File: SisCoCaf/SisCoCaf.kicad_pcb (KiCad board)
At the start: 2 copper layers, 20 parts, among them IC1 LPC111X_102, J1 Conn_01x02_Female, J2 Conn_01x02_Female, J3 Conn_01x03_Male, J4 Conn_01x03_Male, J5 Conn_01x01_Male, Q1 BC547, Q2 BC547, U1 LM317_TO39, U2 NRF24L01_Breakout

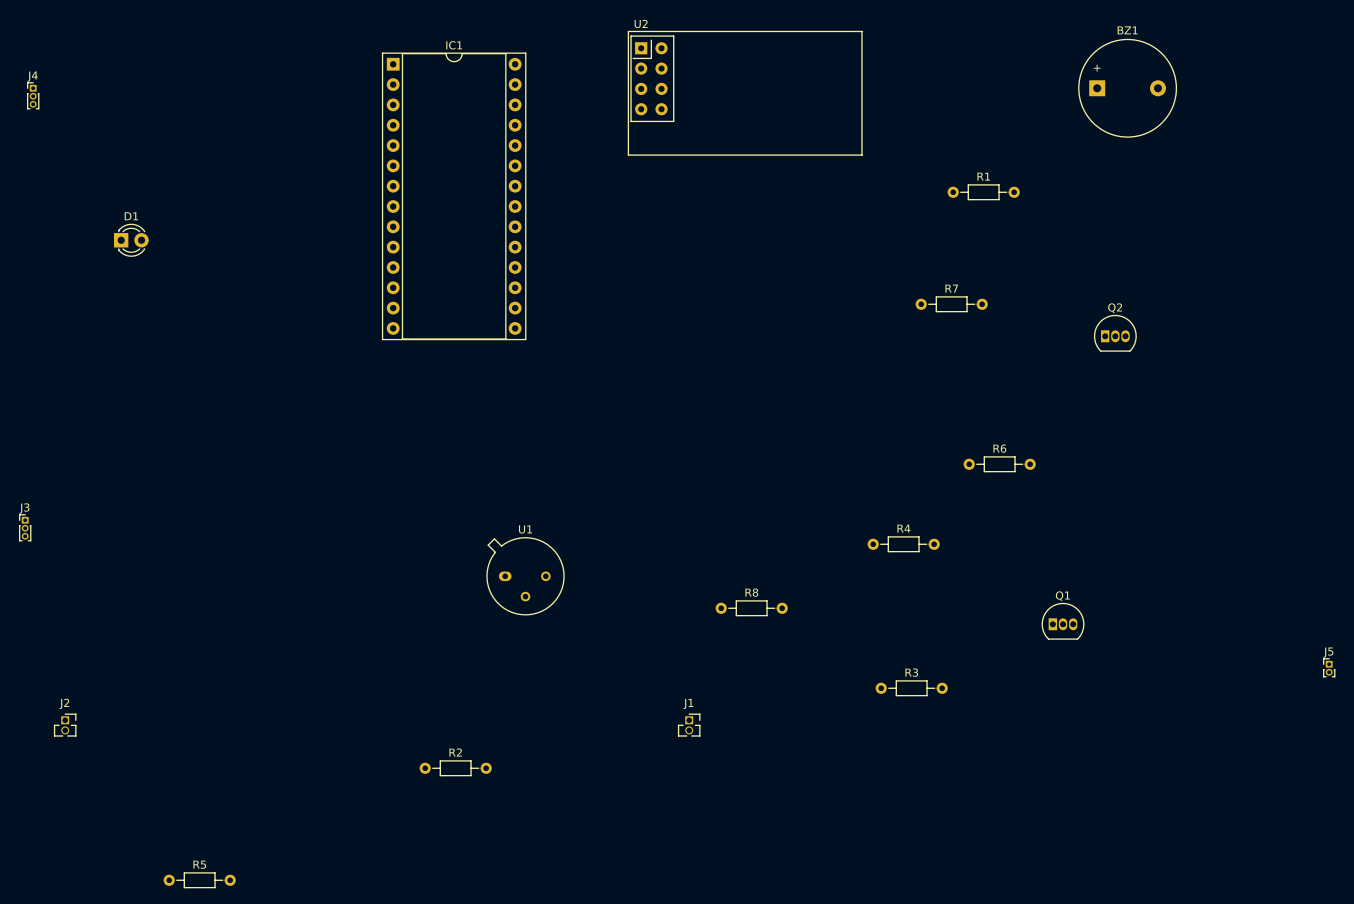
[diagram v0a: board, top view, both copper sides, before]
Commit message: Esquemático corregido. PCB v1.0
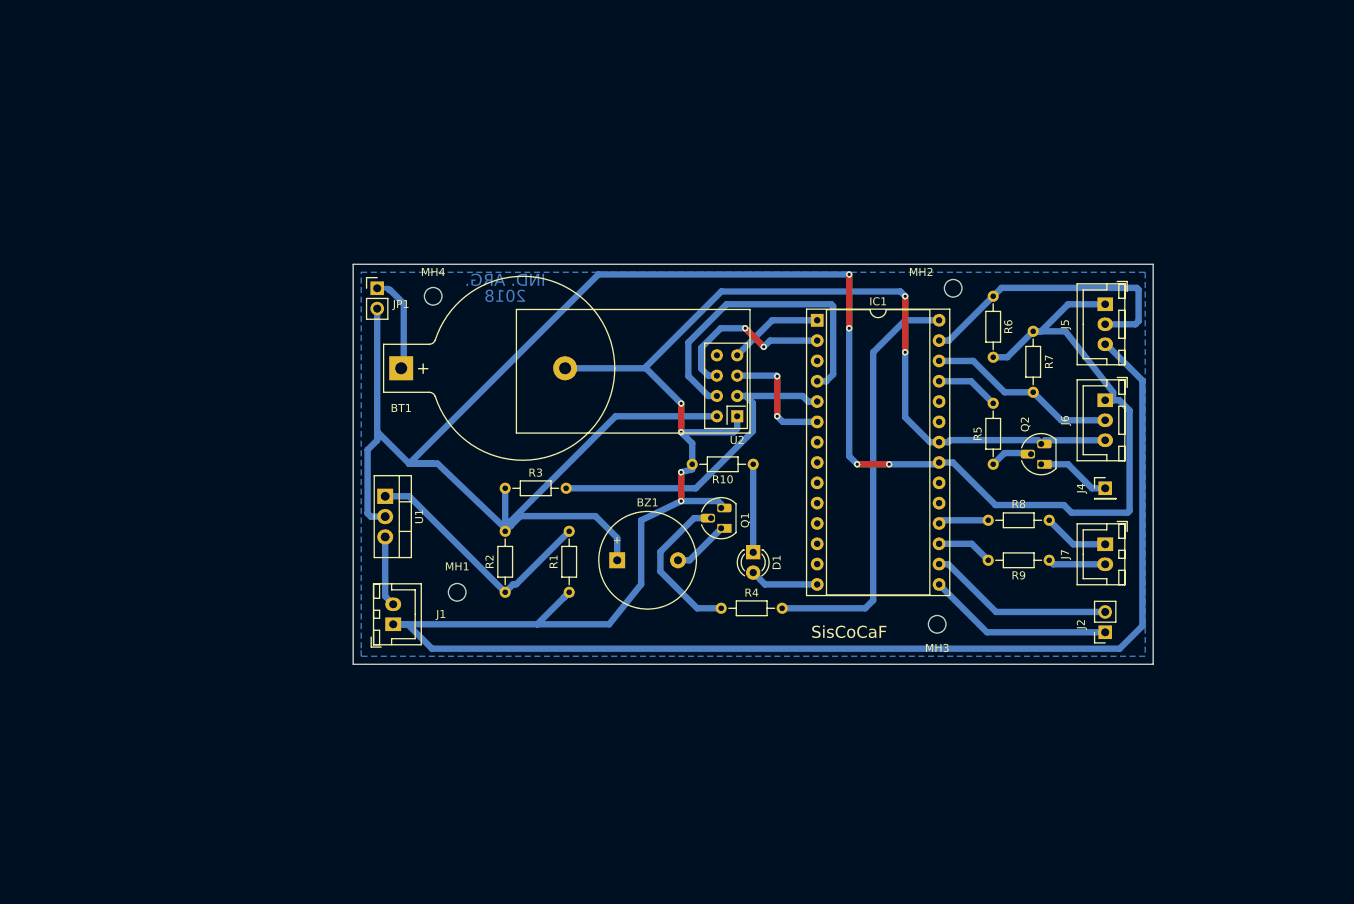
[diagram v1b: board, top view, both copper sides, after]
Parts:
- removed J3: Conn_01x03_Male, Connector_PinHeader_1.00mm:PinHeader_1x03_P1.00mm_Vertical
- added BT1: Battery_Cell, Battery:BatteryHolder_Keystone_103_1x20mm, F.Cu at (99.0, 90.0)
- added J6: Conn_01x03_Male, Connector_JST:JST_XH_B03B-XH-A_1x03_P2.50mm_Vertical, F.Cu at (187.0, 94.0)
- added J7: Conn_01x02_Male, Connector_JST:JST_XH_B02B-XH-A_1x02_P2.50mm_Vertical, F.Cu at (187.0, 112.0)
- added JP1: Jumper, Connector_PinHeader_2.54mm:PinHeader_1x02_P2.54mm_Vertical, F.Cu at (96.0, 80.0)
- added MH1: MountingHole, MountingHole:MountingHole_2.2mm_M2, F.Cu at (106.0, 118.0)
- added MH2: MountingHole, MountingHole:MountingHole_2.2mm_M2, F.Cu at (168.0, 80.0)
- added MH3: MountingHole, MountingHole:MountingHole_2.2mm_M2, F.Cu at (166.0, 122.0)
- added MH4: MountingHole, MountingHole:MountingHole_2.2mm_M2, F.Cu at (103.0, 81.0)
- added R10: 220, Resistor_THT:R_Axial_DIN0204_L3.6mm_D1.6mm_P7.62mm_Horizontal, F.Cu at (143.0, 102.0)
- added R9: 220, Resistor_THT:R_Axial_DIN0204_L3.6mm_D1.6mm_P7.62mm_Horizontal, F.Cu at (180.0, 114.0)
- J1: value Conn_01x02_Female -> Entrada; footprint Connector_PinSocket_1.27mm:PinSocket_1x02_P1.27mm_Vertical -> Connector_JST:JST_XH_B02B-XH-A_1x02_P2.50mm_Vertical
- J2: footprint Connector_PinSocket_1.27mm:PinSocket_1x02_P1.27mm_Vertical -> Connector_PinSocket_2.54mm:PinSocket_1x02_P2.54mm_Vertical
- J4: value Conn_01x03_Male -> Conn_01x01_Male; footprint Connector_PinHeader_1.00mm:PinHeader_1x03_P1.00mm_Vertical -> Connector_PinHeader_2.54mm:PinHeader_1x01_P2.54mm_Vertical
- J5: value Conn_01x01_Male -> Conn_01x03_Male; footprint Connector_PinHeader_1.00mm:PinHeader_1x02_P1.00mm_Vertical -> Connector_JST:JST_XH_B03B-XH-A_1x03_P2.50mm_Vertical
- Q1, Q2: footprint Package_TO_SOT_THT:TO-92_Inline -> Package_TO_SOT_THT:TO-92_HandSolder
- R6, R7: value 220 -> 4k7
- U1: footprint Package_TO_SOT_THT:TO-39-3 -> Package_TO_SOT_THT:TO-220-3_Vertical
- moved J4 143.0 mm to (187.0, 105.0)
- moved J2 130.5 mm to (187.0, 123.0), turned to 180 degrees
- moved R5 115.4 mm to (173.0, 102.0), turned to 90 degrees
- moved D1 88.1 mm to (143.0, 113.0), turned to 270 degrees
- moved BZ1 84.1 mm to (126.0, 114.0)
- moved R1 69.3 mm to (120.0, 118.0), turned to 90 degrees
- moved IC1 61.9 mm to (151.0, 84.0)
- moved R3 53.2 mm to (112.0, 105.0)
- moved J5 53.0 mm to (187.0, 82.0), turned to 270 degrees
- moved U2 47.5 mm to (141.0, 96.0), turned to 180 degrees
- moved Q1 43.2 mm to (139.0, 110.0), turned to 90 degrees
- moved R8 42.4 mm to (180.0, 109.0), turned to 180 degrees
- moved J1 38.9 mm to (98.0, 122.0), turned to 90 degrees
- moved R2 24.2 mm to (112.0, 118.0), turned to 90 degrees
- moved R6 21.2 mm to (173.0, 81.0), turned to 270 degrees
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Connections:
- net Net-(D1-Pad2) renamed /LED
- net Net-(IC1-Pad18) renamed /EntradaD1
- net Net-(IC1-Pad28) renamed /BUZZER
- IC1 pad 15: Net-(IC1-Pad15) -> /RX
- IC1 pad 16: Net-(IC1-Pad16) -> /TX
- IC1 pad 17: Net-(IC1-Pad17) -> /EntradaD2
- IC1 pad 25: Net-(IC1-Pad25) -> /SalidaD1
- IC1 pad 26: Net-(IC1-Pad26) -> /Sensor2
- IC1 pad 27: Net-(IC1-Pad27) -> /Sensor1
- J1 pad 1: Net-(J1-Pad1) -> GND
- J1 pad 2: Net-(J1-Pad2) -> +12V
- J2 pad 1: Net-(IC1-Pad16) -> /RX
- J2 pad 2: Net-(IC1-Pad15) -> /TX
- J4 pad 1: Net-(IC1-Pad27) -> Net-(J4-Pad1)
- J5 pad 1: Net-(J5-Pad1) -> VDD
- J5 pad 2: (no net) -> /Sensor1
- Q2 pad 1: Net-(J5-Pad1) -> Net-(J4-Pad1)
- R5 pad 1: Net-(J1-Pad2) -> Net-(Q2-Pad2)
- R5 pad 2: Net-(IC1-Pad17) -> /SalidaD1
- R6 pad 1: Net-(Q2-Pad2) -> /Sensor1
- R6 pad 2: Net-(IC1-Pad25) -> VDD
- R7 pad 1: Net-(D1-Pad1) -> /Sensor2
- R7 pad 2: GND -> VDD
- R8 pad 1: Net-(J1-Pad1) -> Net-(J7-Pad1)
- U1 pad 1: +12V -> Net-(R1-Pad2)
- U1 pad 2: Net-(R1-Pad2) -> VDD
- U1 pad 3: VDD -> +12V
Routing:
- net GND: track 0.00 -> 310.0 mm, vias 0 -> 6
- net VDD: track 0.00 -> 280.0 mm, vias 0 -> 4
- net /BUZZER: track 0.00 -> 52.7 mm
- net Net-(IC1-Pad5): track 0.00 -> 41.4 mm
- net Net-(IC1-Pad4): track 0.00 -> 39.8 mm
- net /Sensor1: track 0.00 -> 36.0 mm
- net Net-(R1-Pad2): track 0.00 -> 31.1 mm
- net /Sensor2: track 0.00 -> 23.9 mm
- net /RX: track 0.00 -> 23.2 mm
- net /TX: track 0.00 -> 23.0 mm
- net Net-(IC1-Pad2): track 0.00 -> 21.7 mm, vias 0 -> 2
- net Net-(Q1-Pad2): track 0.00 -> 19.6 mm
- net Net-(IC1-Pad6): track 0.00 -> 15.4 mm, vias 0 -> 2
- net Net-(BT1-Pad1): track 0.00 -> 13.4 mm
- net Net-(IC1-Pad1): track 0.00 -> 11.8 mm
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- added copper zone on B.Cu, net GND
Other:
- board outline added: 100 x 50 mm
- net class Default: clearance 0.2 -> 0.8; trace_width 0.25 -> 0.8
- rule trace_clearance: 0.2 -> 0.8
- rule trace_min: 0.2 -> 0.6
- board text added: "2018"
- board text added: "Grilla 1mm. Pista 0.8mm. Margen: 0,8mm. Vías: 0,8mm Agujeros: 2mm. Transferencia por técnica del planchado en una capa."
- board text added: "IND. ARG."
- board text added: "SisCoCaF"

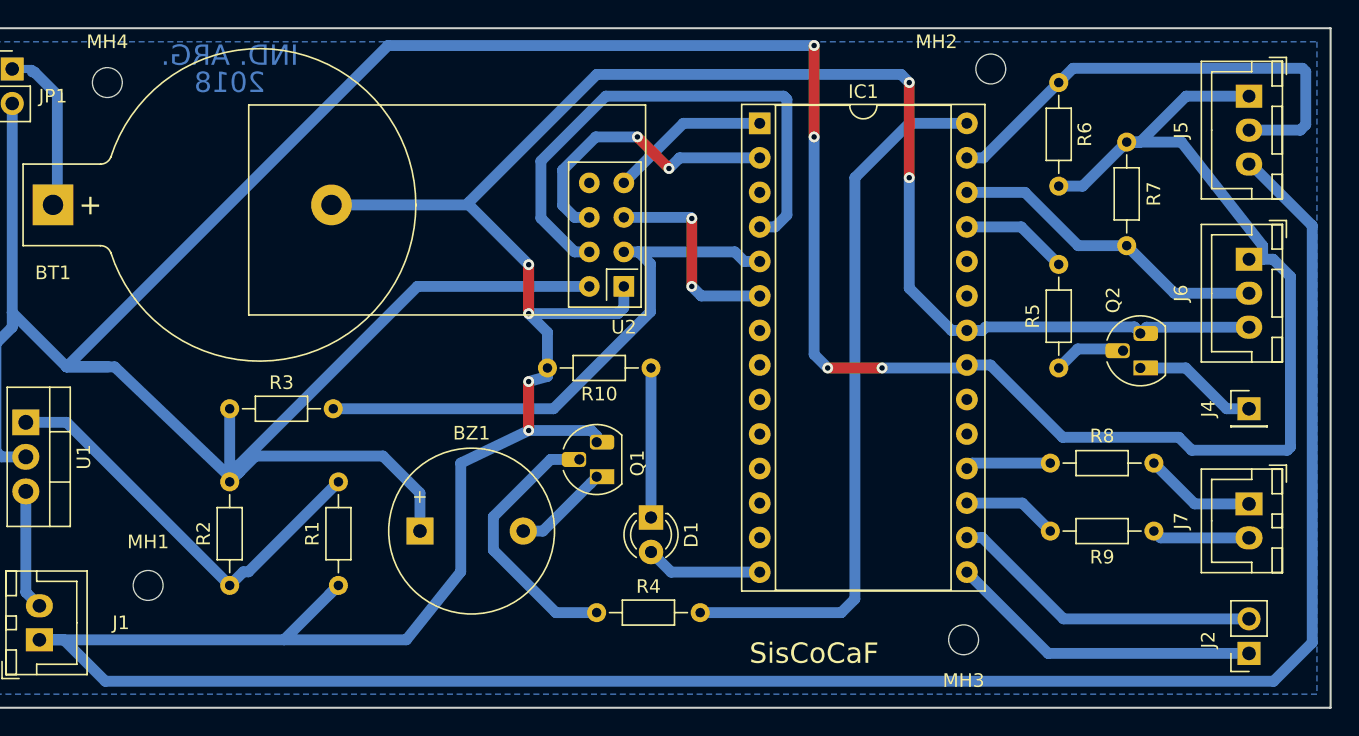
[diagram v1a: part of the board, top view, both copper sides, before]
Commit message: Esquemático y PCB terminados.
En espera de revisión por el profesor.
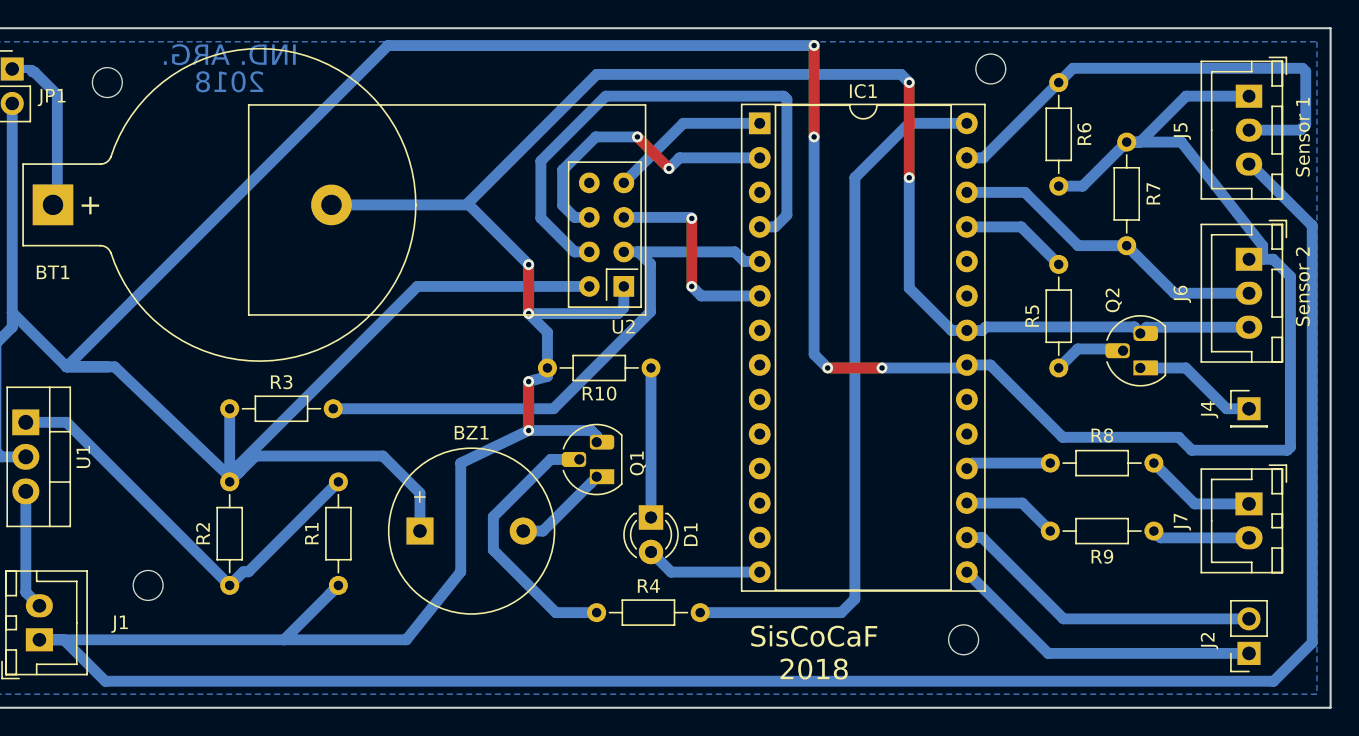
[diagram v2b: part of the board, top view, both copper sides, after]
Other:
- board text added: "Sensor 1"
- board text added: "Sensor 2"
- board text added: "SisCoCaF 2018"
- board text removed: "SisCoCaF"
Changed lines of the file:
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@@
   (general
     (thickness 1.6)
-    (drawings 10)
+    (drawings 12)
     (tracks 200)
     (zones 0)
@@
     (title "SisCoCaf - TP final Diseño de PCB (CESE 2018)")
     (date 2018-11-11)
-    (rev 1.01)
+    (rev 1.02)
     (company "Autor: Roberto Compañy")
-    (comment 1 "PCB del componente 'Nodo'")
-    (comment 2 "Sistema para control sobre la cadena de frío de los medicamentos.")
+    (comment 1 "Licencia Creative Commons")
+    (comment 2 "PCB del componente 'Nodo'.")
+    (comment 3 "Sistema para control sobre la cadena de frío de los medicamentos.")
   )
   (layers
-    (0 F.Cu signal)
-    (31 B.Cu signal)
+    (0 F.Cu signal hide)
+    (31 B.Cu signal hide)
     (32 B.Adhes user)
     (33 F.Adhes user)
@@
     (tags "mounting hole 2.2mm no annular m2")
     (attr virtual)
-    (fp_text reference MH1 (at 0 -3.2) (layer F.SilkS)
+    (fp_text reference MH1 (at 0 -3.2) (layer F.SilkS) hide
       (effects (font (size 1 1) (thickness 0.15)))
     )
@@
     (tags "mounting hole 2.2mm no annular m2")
     (attr virtual)
-    (fp_text reference MH2 (at -4 -2) (layer F.SilkS)
+    (fp_text reference MH2 (at -4 -2) (layer F.SilkS) hide
       (effects (font (size 1 1) (thickness 0.15)))
     )
@@
     (tags "mounting hole 2.2mm no annular m2")
     (attr virtual)
-    (fp_text reference MH3 (at 0 3) (layer F.SilkS)
+    (fp_text reference MH3 (at 0 3) (layer F.SilkS) hide
       (effects (font (size 1 1) (thickness 0.15)))
     )
@@
     (tags "mounting hole 2.2mm no annular m2")
     (attr virtual)
-    (fp_text reference MH4 (at 0 -3) (layer F.SilkS)
+    (fp_text reference MH4 (at 0 -3) (layer F.SilkS) hide
       (effects (font (size 1 1) (thickness 0.15)))
     )
@@
     )
   )
+  (gr_text "Sensor 1" (at 191 85 90) (layer F.SilkS)
+    (effects (font (size 1 1) (thickness 0.15)))
+  )
+  (gr_text "Sensor 2" (at 191 96 90) (layer F.SilkS)
+    (effects (font (size 1 1) (thickness 0.15)))
+  )
   (gr_text "Grilla 1mm.\nPista 0.8mm.\nMargen: 0,8mm.\nVías: 0,8mm\nAgujeros: 2mm.\nTransferencia por técnica del planchado en una capa.\n\n" (at 62 160) (layer Cmts.User)
     (effects (font (size 1.5 1.5) (thickness 0.375)) (justify left))
@@
     (effects (font (size 1.5 1.5) (thickness 0.3)) (justify mirror))
   )
-  (gr_text SisCoCaF (at 155 123) (layer F.SilkS)
+  (gr_text "SisCoCaF\n2018" (at 155 123) (layer F.SilkS)
     (effects (font (size 1.5 1.5) (thickness 0.3)))
   )
